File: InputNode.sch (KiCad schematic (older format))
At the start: 4 parts, among them SW1 SW_Push

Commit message: transered nested project into root and moved docs into docs/ folder
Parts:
- removed SW1: SW_Push, symbol Switch:SW_Push
- added J6: Conn_01x04_Female, Connector_PinSocket_2.54mm:PinSocket_2x02_P2.54mm_Vertical, symbol Connector:Conn_01x04_Female
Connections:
- wire segments 3 -> 7
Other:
- note added: "Footprint\n——————\n| 2 | 1 |\n——————\n| 4 | 3 |\n——————"
- moved on the sheet: D8, R8

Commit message: temp
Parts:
- C1: footprint (none) -> Capacitor_SMD:C_0805_2012Metric_Pad1.15x1.40mm_HandSolder
- R1: footprint (none) -> Resistor_SMD:R_0805_2012Metric_Pad1.15x1.40mm_HandSolder
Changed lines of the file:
@@
 $Descr A4 11693 8268
 encoding utf-8
-Sheet 2 9
+Sheet 3 9
 Title ""
 Date ""
@@
 AR Path="/61554F98/61493944" Ref="R8"  Part="1"
 AR Path="/61555D68/61493944" Ref="R?"  Part="1"
-F 0 "R8" H 7770 4196 50  0000 L CNN
+F 0 "R2" H 7770 4196 50  0000 L CNN
 F 1 "10k" H 7770 4105 50  0000 L CNN
-F 2 "" V 7630 4150 50  0001 C CNN
+F 2 "Resistor_SMD:R_0805_2012Metric_Pad1.15x1.40mm_HandSolder" V 7630 4150 50  0001 C CNN
 F 3 "~" H 7700 4150 50  0001 C CNN
 	1    7700 4150
@@
 AR Path="/61554F98/6149394A" Ref="#PWR050"  Part="1"
 AR Path="/61555D68/6149394A" Ref="#PWR?"  Part="1"
-F 0 "#PWR050" H 7700 4050 50  0001 C CNN
+F 0 "#PWR014" H 7700 4050 50  0001 C CNN
 F 1 "GND" H 7705 4127 50  0000 C CNN
 F 2 "" H 7700 4300 50  0001 C CNN
@@
 AR Path="/61554F98/61493950" Ref="#PWR049"  Part="1"
 AR Path="/61555D68/61493950" Ref="#PWR?"  Part="1"
-F 0 "#PWR049" H 7700 3100 50  0001 C CNN
+F 0 "#PWR013" H 7700 3100 50  0001 C CNN
 F 1 "VDD" H 7715 3423 50  0000 C CNN
 F 2 "" H 7700 3250 50  0001 C CNN
@@
 AR Path="/61554F98/61493958" Ref="D8"  Part="1"
 AR Path="/61555D68/61493958" Ref="D?"  Part="1"
-F 0 "D8" H 5750 4150 50  0000 L CNN
+F 0 "D2" H 5750 4150 50  0000 L CNN
 F 1 "WS2812C" H 5650 4050 50  0000 L CNN
 F 2 "LED_SMD:LED_WS2812B_PLCC4_5.0x5.0mm_P3.2mm" H 5650 3500 50  0001 L TNN
@@
 AR Path="/61554F98/61495684" Ref="#PWR048"  Part="1"
 AR Path="/61555D68/61495684" Ref="#PWR?"  Part="1"
-F 0 "#PWR048" H 5600 3850 50  0001 C CNN
+F 0 "#PWR012" H 5600 3850 50  0001 C CNN
 F 1 "GND" H 5605 3927 50  0000 C CNN
 F 2 "" H 5600 4100 50  0001 C CNN
@@
 AR Path="/61554F98/61495D51" Ref="#PWR047"  Part="1"
 AR Path="/61555D68/61495D51" Ref="#PWR?"  Part="1"
-F 0 "#PWR047" H 5600 3350 50  0001 C CNN
+F 0 "#PWR011" H 5600 3350 50  0001 C CNN
 F 1 "VDD" H 5615 3673 50  0000 C CNN
 F 2 "" H 5600 3500 50  0001 C CNN
@@
 AR Path="/61554F98/614A34FE" Ref="C8"  Part="1"
 AR Path="/61555D68/614A34FE" Ref="C?"  Part="1"
-F 0 "C8" H 4215 3846 50  0000 L CNN
+F 0 "C2" H 4215 3846 50  0000 L CNN
 F 1 "100nF" H 4215 3755 50  0000 L CNN
-F 2 "" H 4138 3650 50  0001 C CNN
+F 2 "Capacitor_SMD:C_0805_2012Metric_Pad1.15x1.40mm_HandSolder" H 4138 3650 50  0001 C CNN
 F 3 "~" H 4100 3800 50  0001 C CNN
 	1    4100 3800
@@
 AR Path="/61554F98/614A4287" Ref="#PWR046"  Part="1"
 AR Path="/61555D68/614A4287" Ref="#PWR?"  Part="1"
-F 0 "#PWR046" H 4100 3700 50  0001 C CNN
+F 0 "#PWR010" H 4100 3700 50  0001 C CNN
 F 1 "GND" H 4105 3777 50  0000 C CNN
 F 2 "" H 4100 3950 50  0001 C CNN
@@
 AR Path="/61554F98/614A4795" Ref="#PWR045"  Part="1"
 AR Path="/61555D68/614A4795" Ref="#PWR?"  Part="1"
-F 0 "#PWR045" H 4100 3500 50  0001 C CNN
+F 0 "#PWR09" H 4100 3500 50  0001 C CNN
 F 1 "VDD" H 4115 3823 50  0000 C CNN
 F 2 "" H 4100 3650 50  0001 C CNN
@@
 AR Path="/61554F92/6156DDAC" Ref="J7"  Part="1"
 AR Path="/61554F98/6156DDAC" Ref="J8"  Part="1"
-F 0 "J8" H 7378 3776 50  0000 L CNN
+F 0 "J2" H 7378 3776 50  0000 L CNN
 F 1 "Conn_01x04_Female" H 7378 3685 50  0000 L CNN
 F 2 "Connector_PinSocket_2.54mm:PinSocket_2x02_P2.54mm_Vertical" H 7350 3800 50  0001 C CNN

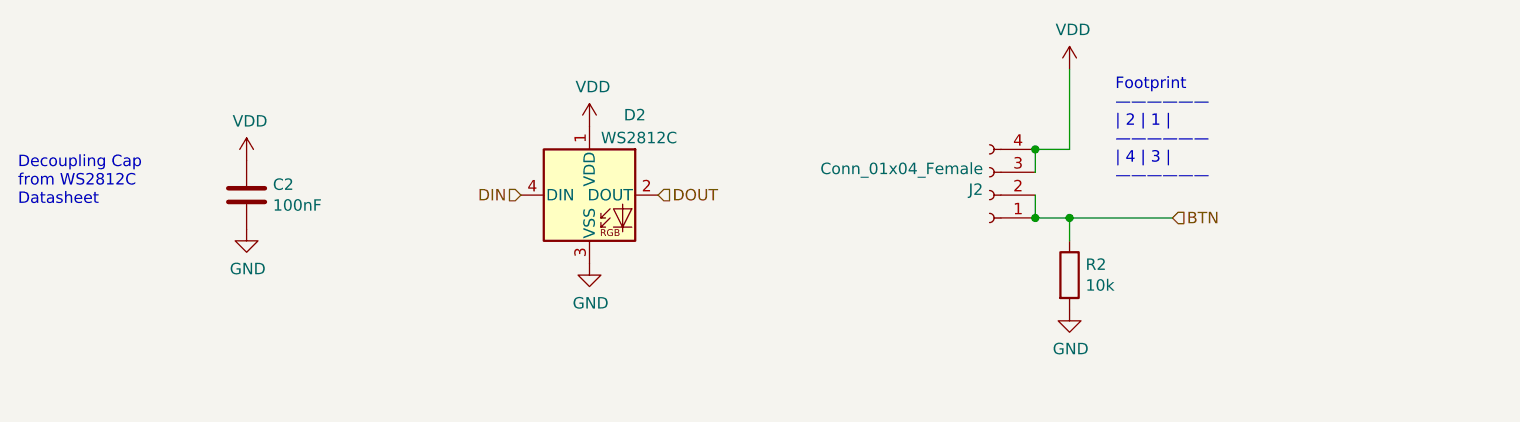
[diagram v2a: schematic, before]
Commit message: updated for homepage
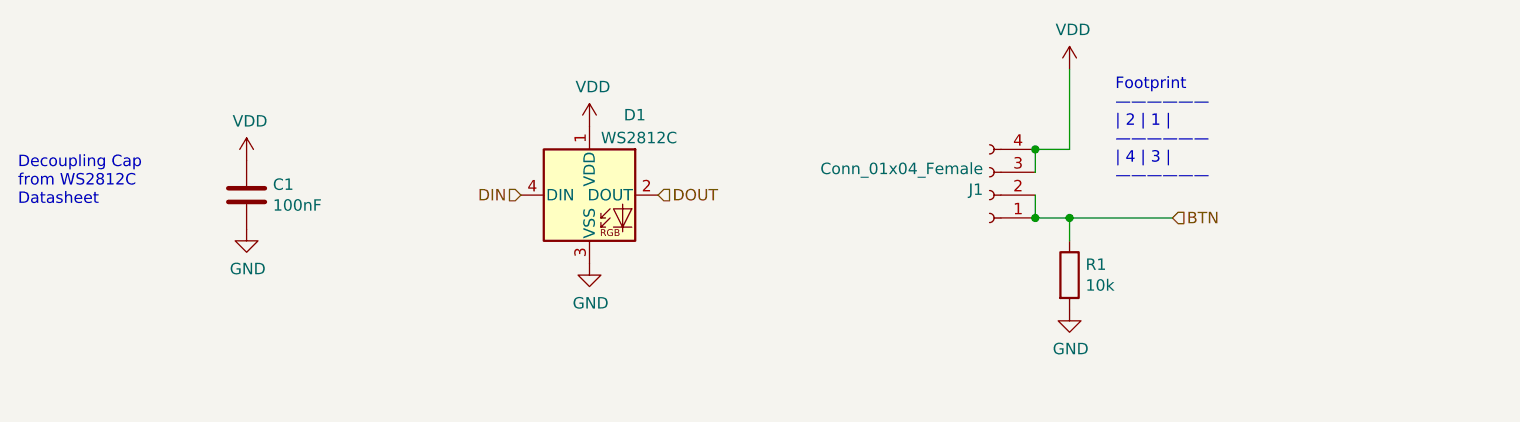
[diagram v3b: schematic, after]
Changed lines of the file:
@@
 $Descr A4 11693 8268
 encoding utf-8
-Sheet 3 9
+Sheet 2 9
 Title ""
 Date ""
@@
 AR Path="/61554F98/61493944" Ref="R8"  Part="1"
 AR Path="/61555D68/61493944" Ref="R?"  Part="1"
-F 0 "R2" H 7770 4196 50  0000 L CNN
+F 0 "R1" H 7770 4196 50  0000 L CNN
 F 1 "10k" H 7770 4105 50  0000 L CNN
 F 2 "Resistor_SMD:R_0805_2012Metric_Pad1.15x1.40mm_HandSolder" V 7630 4150 50  0001 C CNN
@@
 AR Path="/61554F98/6149394A" Ref="#PWR050"  Part="1"
 AR Path="/61555D68/6149394A" Ref="#PWR?"  Part="1"
-F 0 "#PWR014" H 7700 4050 50  0001 C CNN
+F 0 "#PWR06" H 7700 4050 50  0001 C CNN
 F 1 "GND" H 7705 4127 50  0000 C CNN
 F 2 "" H 7700 4300 50  0001 C CNN
@@
 AR Path="/61554F98/61493950" Ref="#PWR049"  Part="1"
 AR Path="/61555D68/61493950" Ref="#PWR?"  Part="1"
-F 0 "#PWR013" H 7700 3100 50  0001 C CNN
+F 0 "#PWR05" H 7700 3100 50  0001 C CNN
 F 1 "VDD" H 7715 3423 50  0000 C CNN
 F 2 "" H 7700 3250 50  0001 C CNN
@@
 AR Path="/61554F98/61493958" Ref="D8"  Part="1"
 AR Path="/61555D68/61493958" Ref="D?"  Part="1"
-F 0 "D2" H 5750 4150 50  0000 L CNN
+F 0 "D1" H 5750 4150 50  0000 L CNN
 F 1 "WS2812C" H 5650 4050 50  0000 L CNN
 F 2 "LED_SMD:LED_WS2812B_PLCC4_5.0x5.0mm_P3.2mm" H 5650 3500 50  0001 L TNN
@@
 AR Path="/61554F98/61495684" Ref="#PWR048"  Part="1"
 AR Path="/61555D68/61495684" Ref="#PWR?"  Part="1"
-F 0 "#PWR012" H 5600 3850 50  0001 C CNN
+F 0 "#PWR04" H 5600 3850 50  0001 C CNN
 F 1 "GND" H 5605 3927 50  0000 C CNN
 F 2 "" H 5600 4100 50  0001 C CNN
@@
 AR Path="/61554F98/61495D51" Ref="#PWR047"  Part="1"
 AR Path="/61555D68/61495D51" Ref="#PWR?"  Part="1"
-F 0 "#PWR011" H 5600 3350 50  0001 C CNN
+F 0 "#PWR03" H 5600 3350 50  0001 C CNN
 F 1 "VDD" H 5615 3673 50  0000 C CNN
 F 2 "" H 5600 3500 50  0001 C CNN
@@
 AR Path="/61554F98/614A34FE" Ref="C8"  Part="1"
 AR Path="/61555D68/614A34FE" Ref="C?"  Part="1"
-F 0 "C2" H 4215 3846 50  0000 L CNN
+F 0 "C1" H 4215 3846 50  0000 L CNN
 F 1 "100nF" H 4215 3755 50  0000 L CNN
 F 2 "Capacitor_SMD:C_0805_2012Metric_Pad1.15x1.40mm_HandSolder" H 4138 3650 50  0001 C CNN
@@
 AR Path="/61554F98/614A4287" Ref="#PWR046"  Part="1"
 AR Path="/61555D68/614A4287" Ref="#PWR?"  Part="1"
-F 0 "#PWR010" H 4100 3700 50  0001 C CNN
+F 0 "#PWR08" H 4100 3700 50  0001 C CNN
 F 1 "GND" H 4105 3777 50  0000 C CNN
 F 2 "" H 4100 3950 50  0001 C CNN
@@
 AR Path="/61554F98/614A4795" Ref="#PWR045"  Part="1"
 AR Path="/61555D68/614A4795" Ref="#PWR?"  Part="1"
-F 0 "#PWR09" H 4100 3500 50  0001 C CNN
+F 0 "#PWR07" H 4100 3500 50  0001 C CNN
 F 1 "VDD" H 4115 3823 50  0000 C CNN
 F 2 "" H 4100 3650 50  0001 C CNN
@@
 AR Path="/61554F92/6156DDAC" Ref="J7"  Part="1"
 AR Path="/61554F98/6156DDAC" Ref="J8"  Part="1"
-F 0 "J2" H 7378 3776 50  0000 L CNN
+F 0 "J1" H 7378 3776 50  0000 L CNN
 F 1 "Conn_01x04_Female" H 7378 3685 50  0000 L CNN
 F 2 "Connector_PinSocket_2.54mm:PinSocket_2x02_P2.54mm_Vertical" H 7350 3800 50  0001 C CNN

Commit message: added resistor network and updated mnt hole footprint
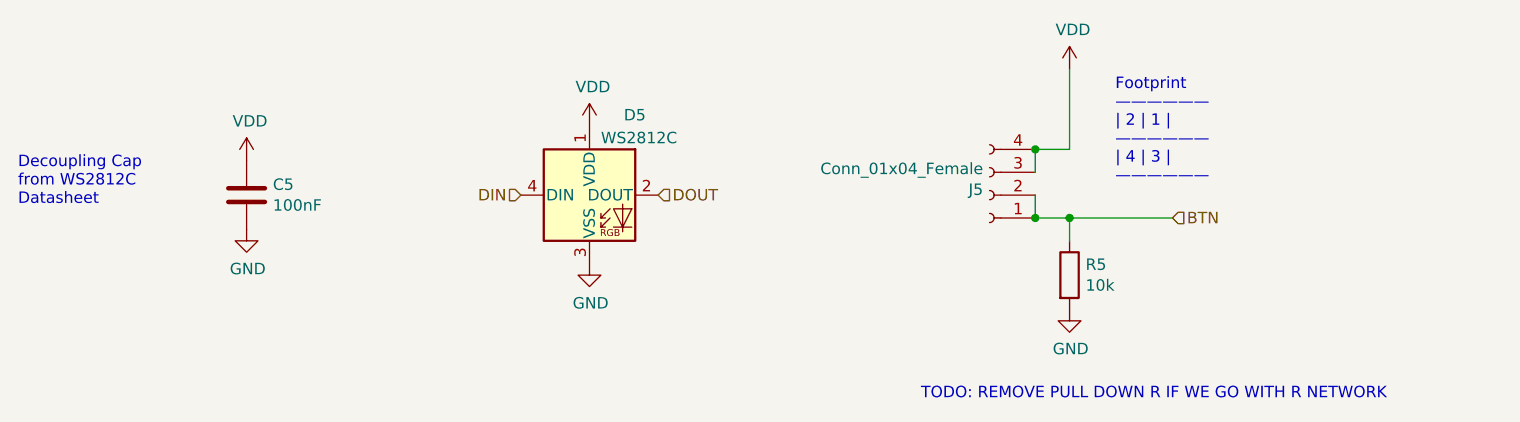
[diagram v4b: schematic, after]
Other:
- note added: "TODO: REMOVE PULL DOWN R IF WE GO WITH R NETWORK"
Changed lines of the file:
@@
 $Descr A4 11693 8268
 encoding utf-8
-Sheet 2 9
+Sheet 6 9
 Title ""
 Date ""
@@
 AR Path="/61554F98/61493944" Ref="R8"  Part="1"
 AR Path="/61555D68/61493944" Ref="R?"  Part="1"
-F 0 "R1" H 7770 4196 50  0000 L CNN
+F 0 "R5" H 7770 4196 50  0000 L CNN
 F 1 "10k" H 7770 4105 50  0000 L CNN
 F 2 "Resistor_SMD:R_0805_2012Metric_Pad1.15x1.40mm_HandSolder" V 7630 4150 50  0001 C CNN
@@
 AR Path="/61554F98/6149394A" Ref="#PWR050"  Part="1"
 AR Path="/61555D68/6149394A" Ref="#PWR?"  Part="1"
-F 0 "#PWR06" H 7700 4050 50  0001 C CNN
+F 0 "#PWR032" H 7700 4050 50  0001 C CNN
 F 1 "GND" H 7705 4127 50  0000 C CNN
 F 2 "" H 7700 4300 50  0001 C CNN
@@
 AR Path="/61554F98/61493950" Ref="#PWR049"  Part="1"
 AR Path="/61555D68/61493950" Ref="#PWR?"  Part="1"
-F 0 "#PWR05" H 7700 3100 50  0001 C CNN
+F 0 "#PWR031" H 7700 3100 50  0001 C CNN
 F 1 "VDD" H 7715 3423 50  0000 C CNN
 F 2 "" H 7700 3250 50  0001 C CNN
@@
 AR Path="/61554F98/61493958" Ref="D8"  Part="1"
 AR Path="/61555D68/61493958" Ref="D?"  Part="1"
-F 0 "D1" H 5750 4150 50  0000 L CNN
+F 0 "D5" H 5750 4150 50  0000 L CNN
 F 1 "WS2812C" H 5650 4050 50  0000 L CNN
 F 2 "LED_SMD:LED_WS2812B_PLCC4_5.0x5.0mm_P3.2mm" H 5650 3500 50  0001 L TNN
@@
 AR Path="/61554F98/61495684" Ref="#PWR048"  Part="1"
 AR Path="/61555D68/61495684" Ref="#PWR?"  Part="1"
-F 0 "#PWR04" H 5600 3850 50  0001 C CNN
+F 0 "#PWR030" H 5600 3850 50  0001 C CNN
 F 1 "GND" H 5605 3927 50  0000 C CNN
 F 2 "" H 5600 4100 50  0001 C CNN
@@
 AR Path="/61554F98/61495D51" Ref="#PWR047"  Part="1"
 AR Path="/61555D68/61495D51" Ref="#PWR?"  Part="1"
-F 0 "#PWR03" H 5600 3350 50  0001 C CNN
+F 0 "#PWR029" H 5600 3350 50  0001 C CNN
 F 1 "VDD" H 5615 3673 50  0000 C CNN
 F 2 "" H 5600 3500 50  0001 C CNN
@@
 AR Path="/61554F98/614A34FE" Ref="C8"  Part="1"
 AR Path="/61555D68/614A34FE" Ref="C?"  Part="1"
-F 0 "C1" H 4215 3846 50  0000 L CNN
+F 0 "C5" H 4215 3846 50  0000 L CNN
 F 1 "100nF" H 4215 3755 50  0000 L CNN
 F 2 "Capacitor_SMD:C_0805_2012Metric_Pad1.15x1.40mm_HandSolder" H 4138 3650 50  0001 C CNN
@@
 AR Path="/61554F98/614A4287" Ref="#PWR046"  Part="1"
 AR Path="/61555D68/614A4287" Ref="#PWR?"  Part="1"
-F 0 "#PWR08" H 4100 3700 50  0001 C CNN
+F 0 "#PWR028" H 4100 3700 50  0001 C CNN
 F 1 "GND" H 4105 3777 50  0000 C CNN
 F 2 "" H 4100 3950 50  0001 C CNN
@@
 AR Path="/61554F98/614A4795" Ref="#PWR045"  Part="1"
 AR Path="/61555D68/614A4795" Ref="#PWR?"  Part="1"
-F 0 "#PWR07" H 4100 3500 50  0001 C CNN
+F 0 "#PWR027" H 4100 3500 50  0001 C CNN
 F 1 "VDD" H 4115 3823 50  0000 C CNN
 F 2 "" H 4100 3650 50  0001 C CNN
@@
 AR Path="/61554F92/6156DDAC" Ref="J7"  Part="1"
 AR Path="/61554F98/6156DDAC" Ref="J8"  Part="1"
-F 0 "J1" H 7378 3776 50  0000 L CNN
+F 0 "J5" H 7378 3776 50  0000 L CNN
 F 1 "Conn_01x04_Female" H 7378 3685 50  0000 L CNN
 F 2 "Connector_PinSocket_2.54mm:PinSocket_2x02_P2.54mm_Vertical" H 7350 3800 50  0001 C CNN
@@
 	7700 3900 8150 3900
 Connection ~ 7700 3900
+Text Notes 7050 4700 0    50   ~ 0
+TODO: REMOVE PULL DOWN R IF WE GO WITH R NETWORK
 $EndSCHEMATC

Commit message: PCB layout updates
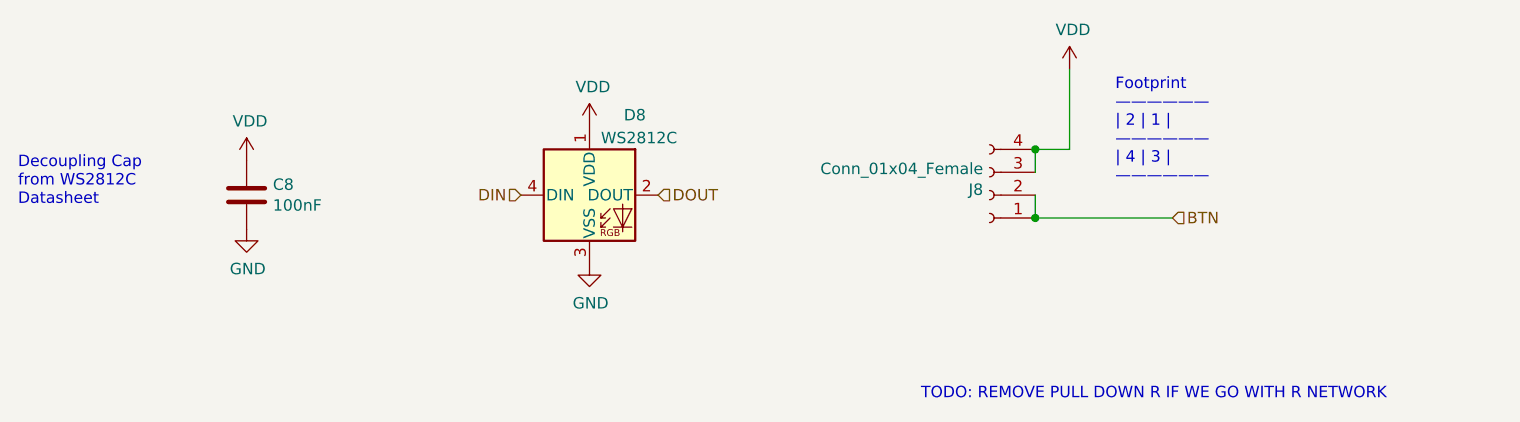
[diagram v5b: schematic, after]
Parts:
- removed R1: 10k, Resistor_SMD:R_0805_2012Metric_Pad1.15x1.40mm_HandSolder, symbol Device:R
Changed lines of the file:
@@
 $Descr A4 11693 8268
 encoding utf-8
-Sheet 6 9
+Sheet 9 9
 Title ""
 Date ""
@@
 Comment4 ""
 $EndDescr
-$Comp
-L Device:R R?
-U 1 1 61493944
-P 7700 4150
-AR Path="/61493944" Ref="R?"  Part="1"
-AR Path="/6149038E/61493944" Ref="R1"  Part="1"
-AR Path="/614A08BA/61493944" Ref="R2"  Part="1"
-AR Path="/61551931/61493944" Ref="R3"  Part="1"
-AR Path="/6155214B/61493944" Ref="R4"  Part="1"
-AR Path="/61552612/61493944" Ref="R5"  Part="1"
-AR Path="/61552B2D/61493944" Ref="R6"  Part="1"
-AR Path="/61553054/61493944" Ref="R?"  Part="1"
-AR Path="/61554F92/61493944" Ref="R7"  Part="1"
-AR Path="/61554F98/61493944" Ref="R8"  Part="1"
-AR Path="/61555D68/61493944" Ref="R?"  Part="1"
-F 0 "R5" H 7770 4196 50  0000 L CNN
-F 1 "10k" H 7770 4105 50  0000 L CNN
-F 2 "Resistor_SMD:R_0805_2012Metric_Pad1.15x1.40mm_HandSolder" V 7630 4150 50  0001 C CNN
-F 3 "~" H 7700 4150 50  0001 C CNN
-	1    7700 4150
-	1    0    0    -1
-$EndComp
-$Comp
-L power:GND #PWR?
-U 1 1 6149394A
-P 7700 4300
-AR Path="/6149394A" Ref="#PWR?"  Part="1"
-AR Path="/6149038E/6149394A" Ref="#PWR06"  Part="1"
-AR Path="/614A08BA/6149394A" Ref="#PWR014"  Part="1"
-AR Path="/61551931/6149394A" Ref="#PWR020"  Part="1"
-AR Path="/6155214B/6149394A" Ref="#PWR026"  Part="1"
-AR Path="/61552612/6149394A" Ref="#PWR032"  Part="1"
-AR Path="/61552B2D/6149394A" Ref="#PWR038"  Part="1"
-AR Path="/61553054/6149394A" Ref="#PWR?"  Part="1"
-AR Path="/61554F92/6149394A" Ref="#PWR044"  Part="1"
-AR Path="/61554F98/6149394A" Ref="#PWR050"  Part="1"
-AR Path="/61555D68/6149394A" Ref="#PWR?"  Part="1"
-F 0 "#PWR032" H 7700 4050 50  0001 C CNN
-F 1 "GND" H 7705 4127 50  0000 C CNN
-F 2 "" H 7700 4300 50  0001 C CNN
-F 3 "" H 7700 4300 50  0001 C CNN
-	1    7700 4300
-	1    0    0    -1
-$EndComp
 $Comp
 L power:VDD #PWR?
@@
 AR Path="/61554F98/61493950" Ref="#PWR049"  Part="1"
 AR Path="/61555D68/61493950" Ref="#PWR?"  Part="1"
-F 0 "#PWR031" H 7700 3100 50  0001 C CNN
+F 0 "#PWR049" H 7700 3100 50  0001 C CNN
 F 1 "VDD" H 7715 3423 50  0000 C CNN
 F 2 "" H 7700 3250 50  0001 C CNN
@@
 AR Path="/61554F98/61493958" Ref="D8"  Part="1"
 AR Path="/61555D68/61493958" Ref="D?"  Part="1"
-F 0 "D5" H 5750 4150 50  0000 L CNN
+F 0 "D8" H 5750 4150 50  0000 L CNN
 F 1 "WS2812C" H 5650 4050 50  0000 L CNN
 F 2 "LED_SMD:LED_WS2812B_PLCC4_5.0x5.0mm_P3.2mm" H 5650 3500 50  0001 L TNN
@@
 AR Path="/61554F98/61495684" Ref="#PWR048"  Part="1"
 AR Path="/61555D68/61495684" Ref="#PWR?"  Part="1"
-F 0 "#PWR030" H 5600 3850 50  0001 C CNN
+F 0 "#PWR048" H 5600 3850 50  0001 C CNN
 F 1 "GND" H 5605 3927 50  0000 C CNN
 F 2 "" H 5600 4100 50  0001 C CNN
@@
 AR Path="/61554F98/61495D51" Ref="#PWR047"  Part="1"
 AR Path="/61555D68/61495D51" Ref="#PWR?"  Part="1"
-F 0 "#PWR029" H 5600 3350 50  0001 C CNN
+F 0 "#PWR047" H 5600 3350 50  0001 C CNN
 F 1 "VDD" H 5615 3673 50  0000 C CNN
 F 2 "" H 5600 3500 50  0001 C CNN
@@
 AR Path="/61554F98/614A34FE" Ref="C8"  Part="1"
 AR Path="/61555D68/614A34FE" Ref="C?"  Part="1"
-F 0 "C5" H 4215 3846 50  0000 L CNN
+F 0 "C8" H 4215 3846 50  0000 L CNN
 F 1 "100nF" H 4215 3755 50  0000 L CNN
 F 2 "Capacitor_SMD:C_0805_2012Metric_Pad1.15x1.40mm_HandSolder" H 4138 3650 50  0001 C CNN
@@
 AR Path="/61554F98/614A4287" Ref="#PWR046"  Part="1"
 AR Path="/61555D68/614A4287" Ref="#PWR?"  Part="1"
-F 0 "#PWR028" H 4100 3700 50  0001 C CNN
+F 0 "#PWR046" H 4100 3700 50  0001 C CNN
 F 1 "GND" H 4105 3777 50  0000 C CNN
 F 2 "" H 4100 3950 50  0001 C CNN
@@
 AR Path="/61554F98/614A4795" Ref="#PWR045"  Part="1"
 AR Path="/61555D68/614A4795" Ref="#PWR?"  Part="1"
-F 0 "#PWR027" H 4100 3500 50  0001 C CNN
+F 0 "#PWR045" H 4100 3500 50  0001 C CNN
 F 1 "VDD" H 4115 3823 50  0000 C CNN
 F 2 "" H 4100 3650 50  0001 C CNN
@@
 AR Path="/61554F92/6156DDAC" Ref="J7"  Part="1"
 AR Path="/61554F98/6156DDAC" Ref="J8"  Part="1"
-F 0 "J5" H 7378 3776 50  0000 L CNN
+F 0 "J8" H 7378 3776 50  0000 L CNN
 F 1 "Conn_01x04_Female" H 7378 3685 50  0000 L CNN
 F 2 "Connector_PinSocket_2.54mm:PinSocket_2x02_P2.54mm_Vertical" H 7350 3800 50  0001 C CNN
@@
 	7550 3600 7700 3600
 Connection ~ 7550 3600
-Wire Wire Line
-	7550 3900 7700 3900
-Wire Wire Line
-	7700 3900 7700 4000
 Connection ~ 7550 3900
-Wire Wire Line
-	7700 3900 8150 3900
-Connection ~ 7700 3900
 Text Notes 7050 4700 0    50   ~ 0
 TODO: REMOVE PULL DOWN R IF WE GO WITH R NETWORK
+Wire Wire Line
+	7550 3900 8150 3900
 $EndSCHEMATC
